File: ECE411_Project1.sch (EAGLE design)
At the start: 13 parts

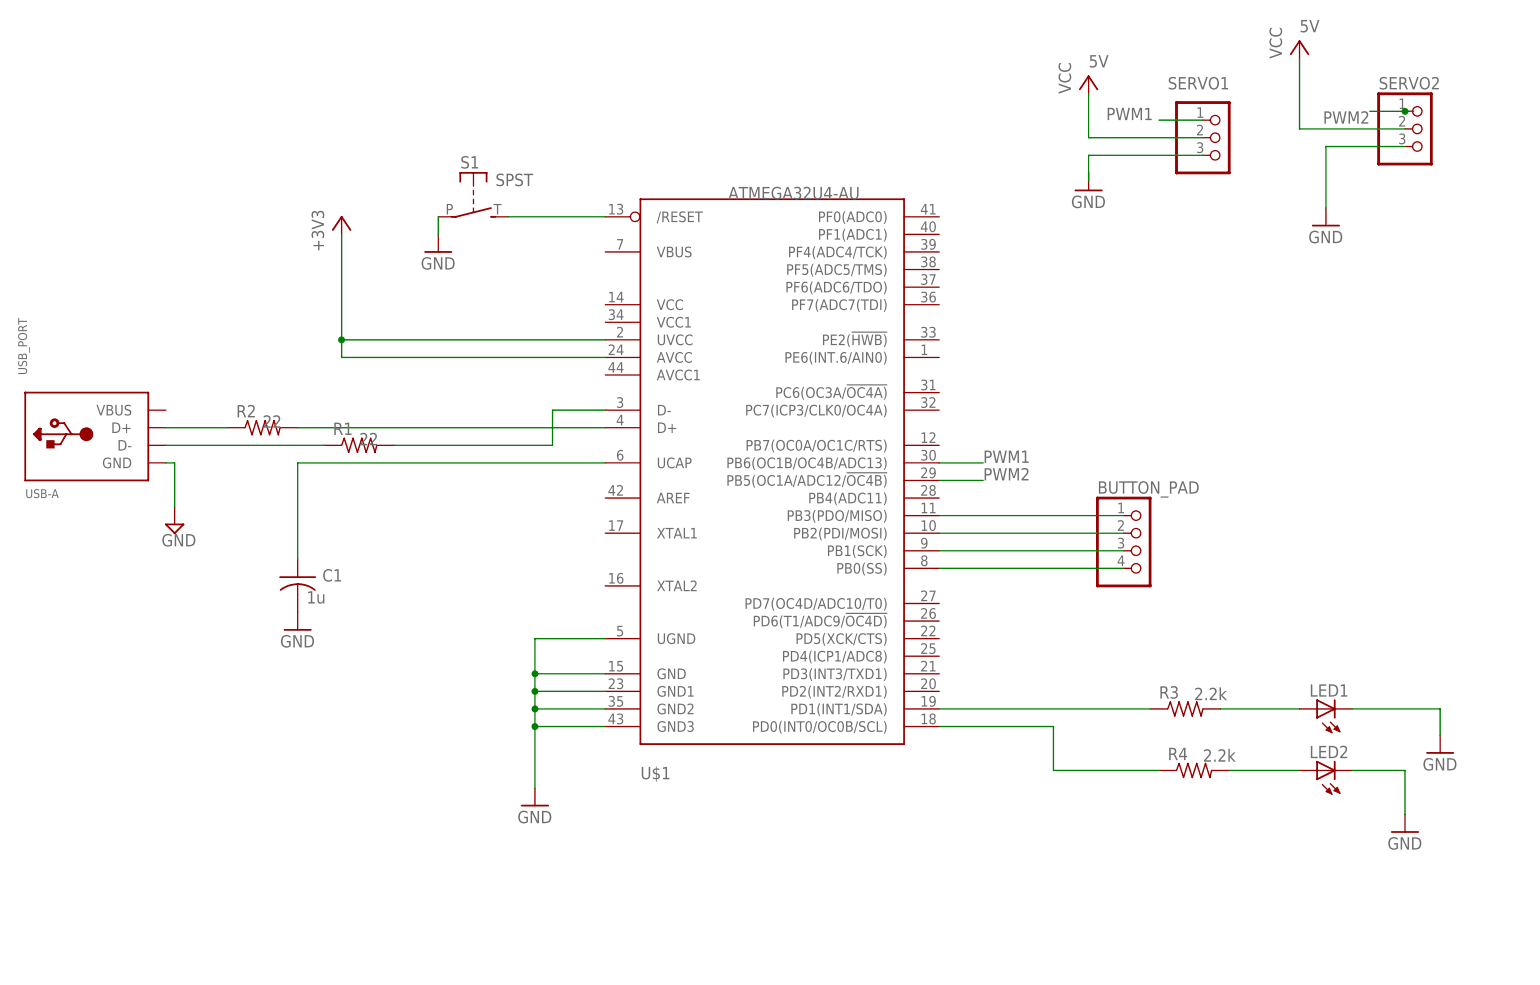
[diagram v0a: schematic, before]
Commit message: Beautified the circuit: rotated and connected the servos directly to the ATMega32U4
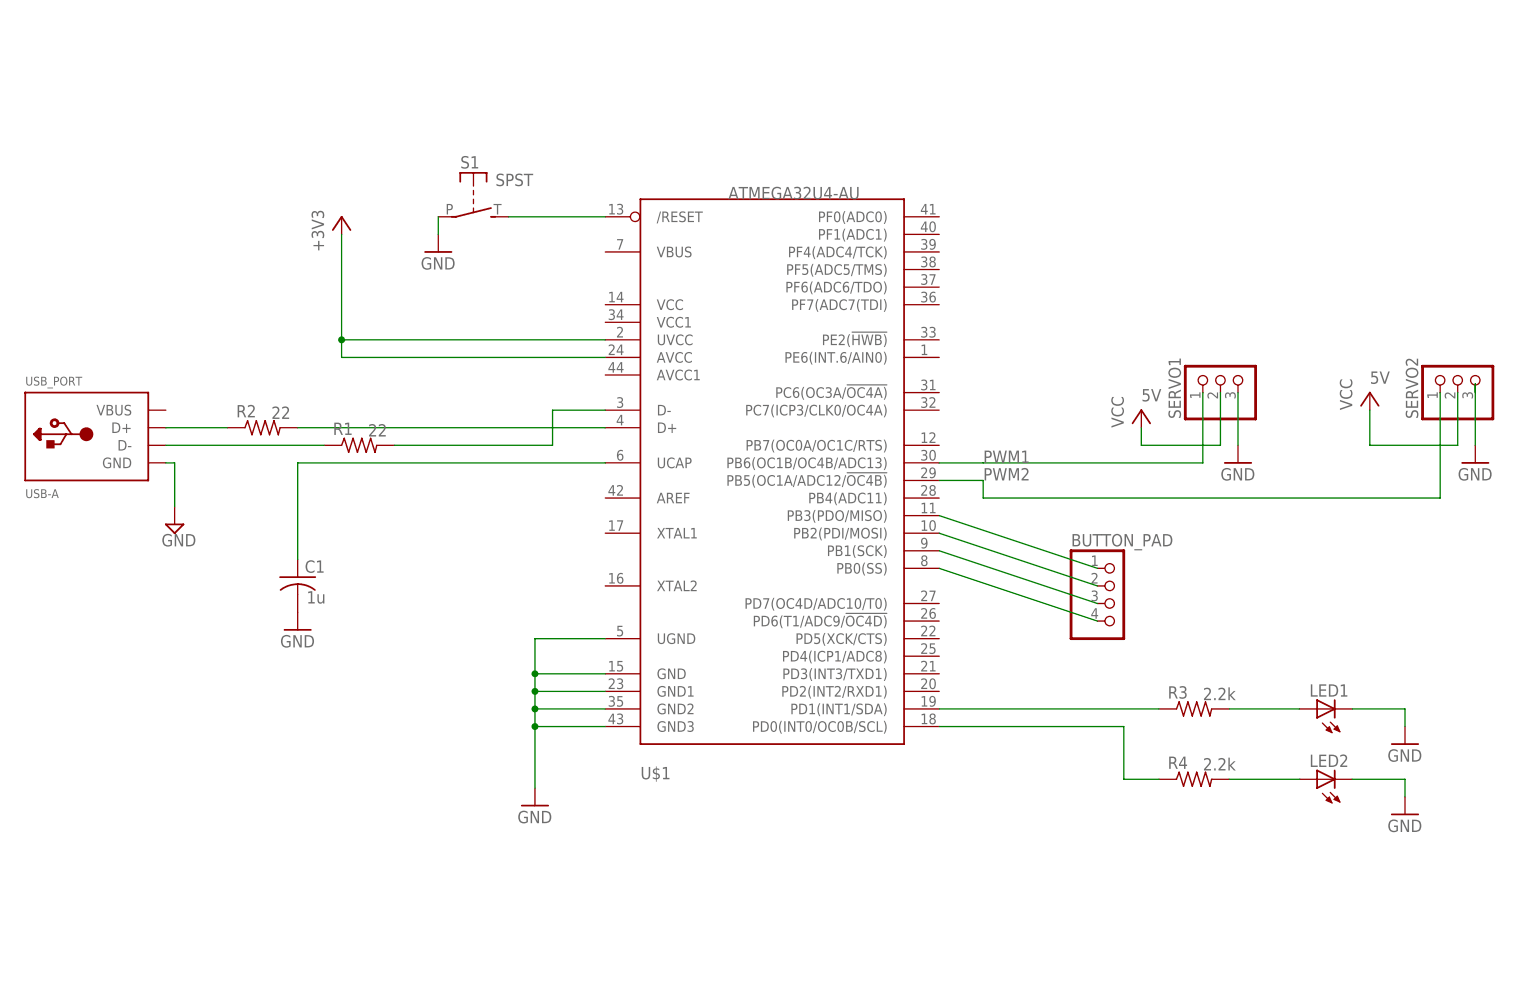
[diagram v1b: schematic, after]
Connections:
- removed net N$15: SERVO1.1
- net PWM1: now also SERVO1.1
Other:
- moved on the sheet: BUTTON_PAD, LED2, R3, R4, SERVO1, SERVO2

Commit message: Added ISP 6-pin port to the schematic
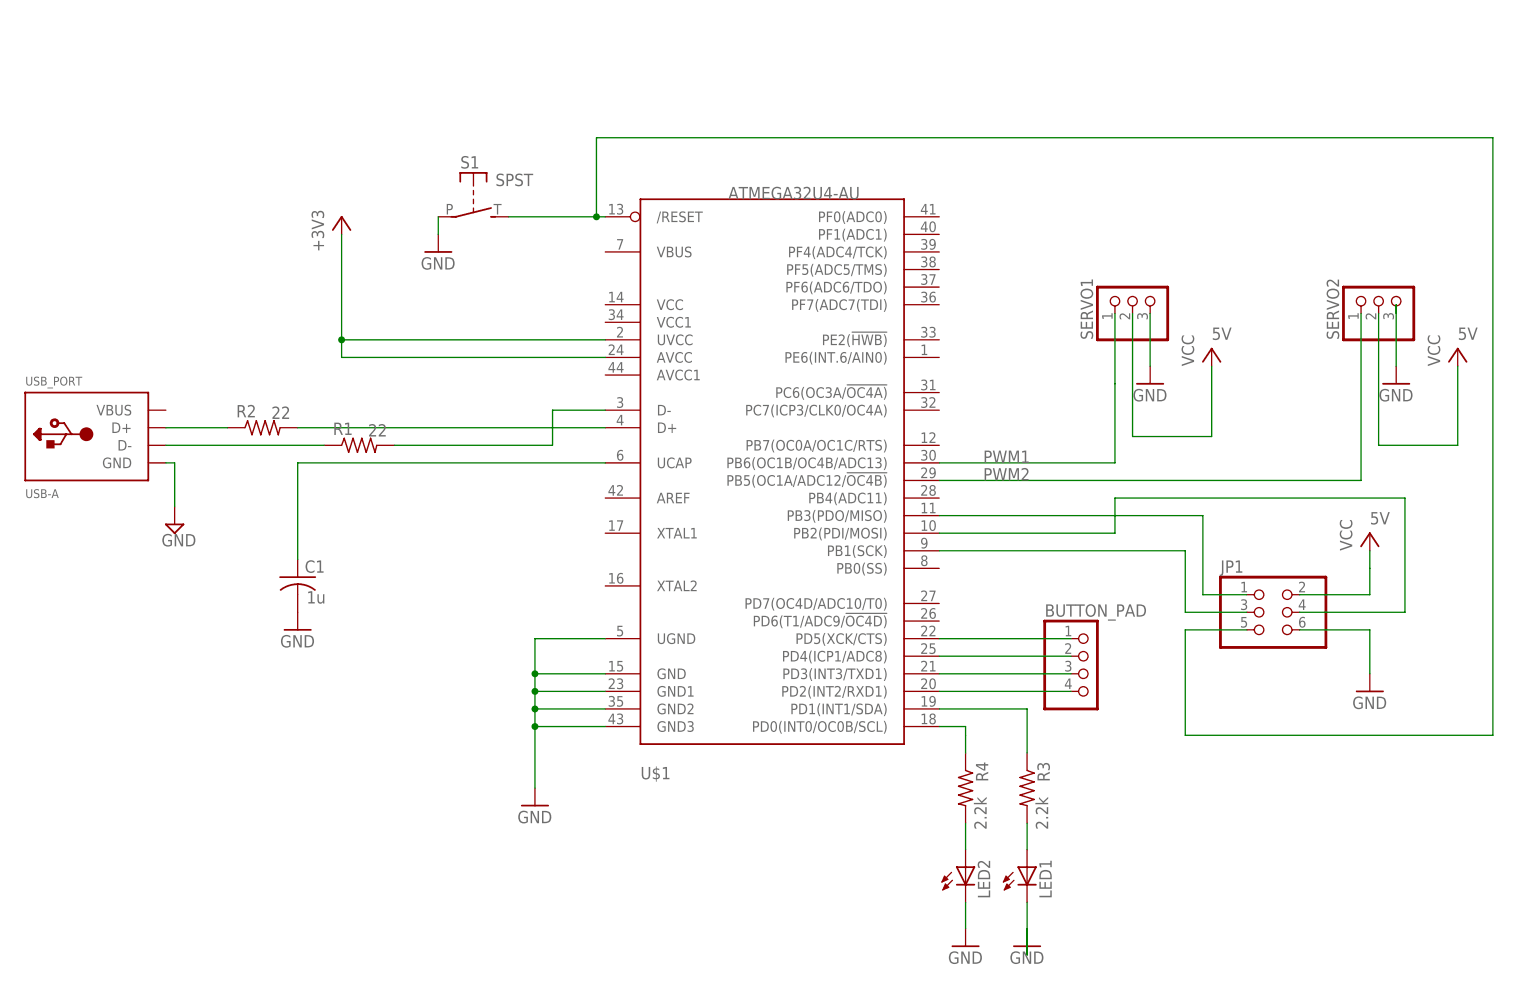
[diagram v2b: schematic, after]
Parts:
- added JP1: (no value), pinhead:PINHD-2X3
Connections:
- new net N$15: JP1.2
- new net N$16: JP1.1, U$1.PB3(PDO/MISO)
- new net N$17: JP1.4, U$1.PB2(PDI/MOSI)
- new net N$18: JP1.3, U$1.PB1(SCK)
- net GND: now also JP1.6
- net N$11: now also U$1.PD3(INT3/TXD1); no longer U$1.PB1(SCK)
- net N$12: now also U$1.PD4(ICP1/ADC8); no longer U$1.PB2(PDI/MOSI)
- net N$13: now also U$1.PD5(XCK/CTS); no longer U$1.PB3(PDO/MISO)
- net N$14: now also JP1.5
- net N$7: now also U$1.PD2(INT2/RXD1); no longer U$1.PB0(SS)
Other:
- moved on the sheet: BUTTON_PAD, LED1, LED2, R3, R4, SERVO1, SERVO2

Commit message: In-Progress schematic: working to add voltage regulators
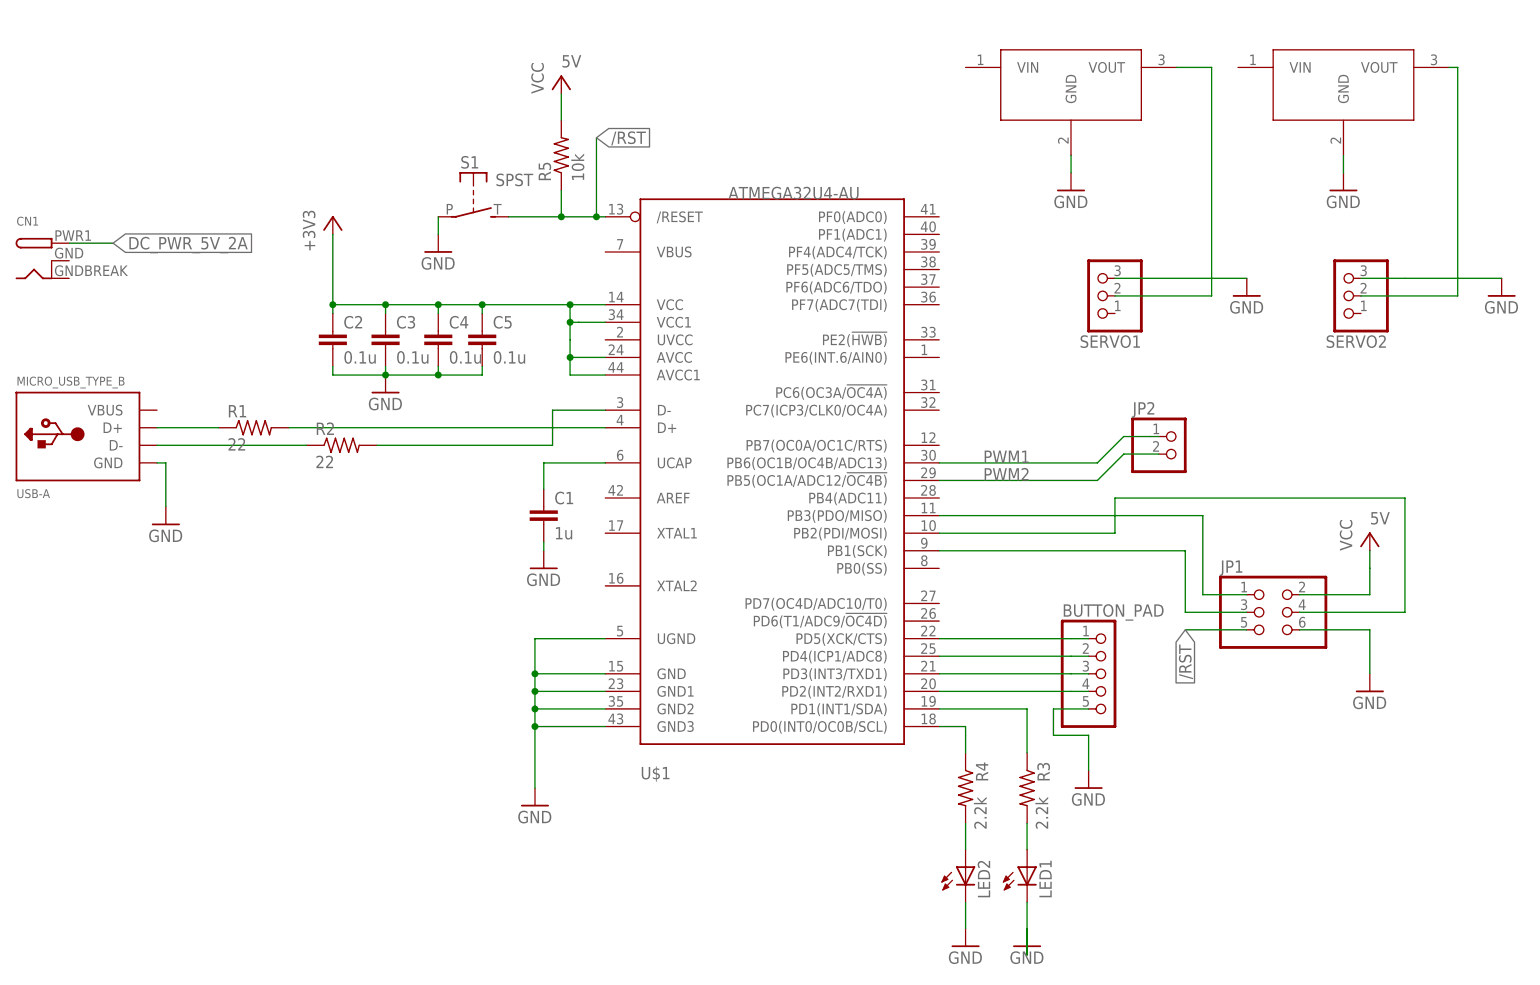
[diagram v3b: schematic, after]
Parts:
- removed USB_PORT: USB-A, adafruit:USB-A
- added 5V1A_REGULATOR1, 5V1A_REGULATOR2: L7805ABV, L7805ABV:L7805ABV
- added C2, C3, C4, C5: 0.1u, rcl:C-EUC1206
- added CN1: (no value), adafruit:DCBARRELSMT
- added JP2: (no value), pinhead:PINHD-1X2
- added MICRO_USB_TYPE_B: USB-A, adafruit:USB-A
- added R5: 10k, rcl:R-US_R1206
- BUTTON_PAD: device pinhead:PINHD-1X4 -> pinhead:PINHD-1X5
- C1: value (none) -> 1u; device rcl:C-US025-024X044 -> rcl:C-EUC1206; SPICEPREFIX 1u -> (none)
- R1, R2: value (none) -> 22; device rcl:R-US_0204/7 -> rcl:R-US_R1206; SPICEPREFIX 22 -> (none)
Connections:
- new net /RST: JP1.5, R5.1, S1.S, U$1./RESET
- new net DC_PWR_5V_2A: CN1.PWR
- new net N$19: 5V1A_REGULATOR2.VOUT, SERVO2.2
- net +3V3: now also C2.1, C3.1, C4.1, C5.1, U$1.AVCC1, U$1.VCC, U$1.VCC1; no longer U$1.UVCC
- net GND: now also 5V1A_REGULATOR1.GND, 5V1A_REGULATOR2.GND, BUTTON_PAD.5, C2.2, C3.2, C4.2, C5.2, MICRO_USB_TYPE_B.GND; no longer USB_PORT.GND
- net N$1: now also MICRO_USB_TYPE_B.D+, R1.1; no longer R2.1, USB_PORT.D+
- net N$14: now also 5V1A_REGULATOR1.VOUT, SERVO1.2; no longer JP1.5, S1.S, U$1./RESET
- net N$2: now also R1.2; no longer R2.2
- net N$3: now also MICRO_USB_TYPE_B.D-, R2.1; no longer R1.1, USB_PORT.D-
- net N$4: now also R2.2; no longer R1.2
- net PWM1: now also JP2.1; no longer SERVO1.1
- net PWM2: now also JP2.2; no longer SERVO2.1
- net VCC: now also R5.2; no longer SERVO1.2, SERVO2.2
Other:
- moved on the sheet: C1, R1, R2, SERVO1, SERVO2
